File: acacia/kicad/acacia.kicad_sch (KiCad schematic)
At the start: 123 parts, among them J1 USB_C, SW1 A, SW10 C, SW11 R, SW12 F, SW13 V, SW14 T, SW15 G, SW16 Back, SW17 Gui, SW18 Ctl, SW19 Alt, SW2 Z, SW20 Sft, SW21 Fwd, SW22 AltGr, SW23 L1, SW24 L2, SW25 Ctl, SW26 U, SW27 J, SW28 M, SW29 H, SW3 Esc, SW30 N, SW31 I, SW32 K, SW33 Comm, SW34 O, SW35 L, SW36 Dot, SW37 QMK, SW38 P, SW39 Semi, SW4 B, SW40 Slsh, SW41 Y, SW42 Png, SW43 RESET, SW48 Q, SW49 RESET, SW5 W, SW6 S, SW7 X, SW8 E, SW9 D, U1 USBLC6-2SC6, U2 ATmega32U2-A, Y1 16MHz

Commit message: rearrange
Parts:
- removed FL1: CommonMode, symbol the_tree:Filter_EMI_CommonMode
- removed J1: USB_C, symbol Connector:USB_C_Receptacle_USB2.0
- removed SW37: QMK, symbol Switch:SW_Push_45deg
- added FL1: NCC0805F900KTRF, Inductor_SMD:L_CommonModeChoke_Coilcraft_0805USB, symbol mech-kbd:Filter_EMI_CommonMode
- added J1: USB4500-03-0-A, mech-kbd:USB4500030A, symbol mech-kbd:USB4500-03-0-A
- C1, C2, C3, C4, C5, C7, C8: footprint (none) -> Capacitor_SMD:C_0805_2012Metric_Pad1.18x1.45mm_HandSolder
- C6: footprint (none) -> Capacitor_SMD:C_1206_3216Metric_Pad1.33x1.80mm_HandSolder
- D1, D10, D11, D12, D13, D14, D15, D16, D17, D18, D19, D2, D20, D21, D22, D23, D24, D25, D26, D27, D28, D29, D3, D30, D31, D32, D33, D34, D35, D36, D37, D38, D39, D4, D40, D41, D48, D5, D6, D7, D8, D9: footprint (none) -> Diode_SMD:D_0805_2012Metric_Pad1.15x1.40mm_HandSolder
- F1: footprint (none) -> Resistor_SMD:R_1210_3225Metric_Pad1.30x2.65mm_HandSolder
- FB1, FB2, R1, R2, R3, R4, R5, R6, R7, R8: footprint (none) -> Resistor_SMD:R_0805_2012Metric_Pad1.20x1.40mm_HandSolder
- SW1, SW10, SW11, SW12, SW13, SW14, SW15, SW16, SW17, SW2, SW20, SW21, SW22, SW25, SW26, SW27, SW28, SW29, SW3, SW30, SW31, SW32, SW33, SW34, SW35, SW36, SW38, SW39, SW4, SW40, SW41, SW42, SW48, SW5, SW6, SW7, SW8, SW9: footprint (none) -> mech-kbd:MX-Hotswap-1U
- SW18, SW23, Y1: footprint (none) -> mech-kbd:MX-Hotswap-1.5U
- SW19, SW24: footprint (none) -> mech-kbd:MX-Hotswap-1.25U
- SW43: value RESET -> QMK; footprint (none) -> Button_Switch_SMD:SW_SPST_EVQQ2
- SW49: footprint (none) -> Button_Switch_SMD:SW_SPST_EVQQ2
- TP1, TP2: footprint (none) -> TestPoint:TestPoint_Pad_1.0x1.0mm
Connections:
- net D+: now also J1.A6 (DP1), J1.B6 (DP2)
- net D-: now also J1.A7 (DN1), J1.B7 (DN2)
- net DD+: now also FL1.4
- net DD-: now also FL1.1
- net GND: now also J1.A1 (GND_1), J1.A12 (GND_2)
- net GNDPWR: now also J1.MH1, J1.MH2, J1.MH3, J1.MH4
- net VBUS: now reaches FB2.1, U1.5 (VBUS)
- net VBUS: now also J1.A4 (VBUS_1), J1.A9 (VBUS_2)
- net at R8.1: now also J1.B5 (CC2)
- net at R7.1: now also J1.A5 (CC1)
- net at R3.1: now also FL1.2
- net at R2.1: now also FL1.3
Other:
- moved on the sheet: H1

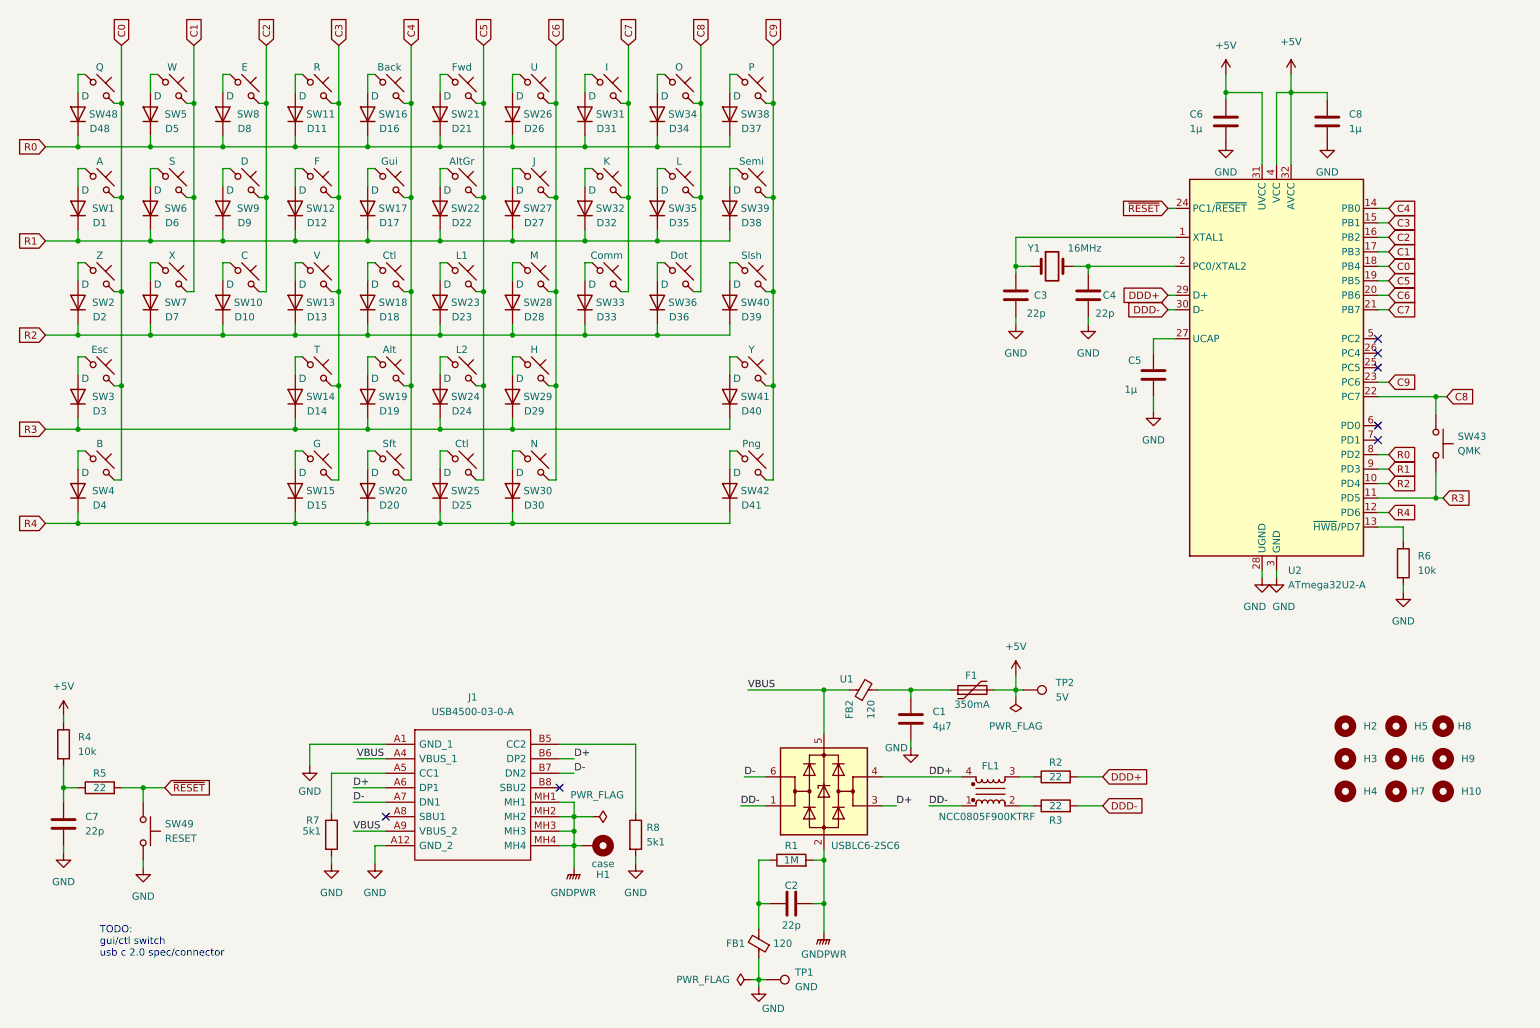
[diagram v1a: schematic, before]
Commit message: keys layed out
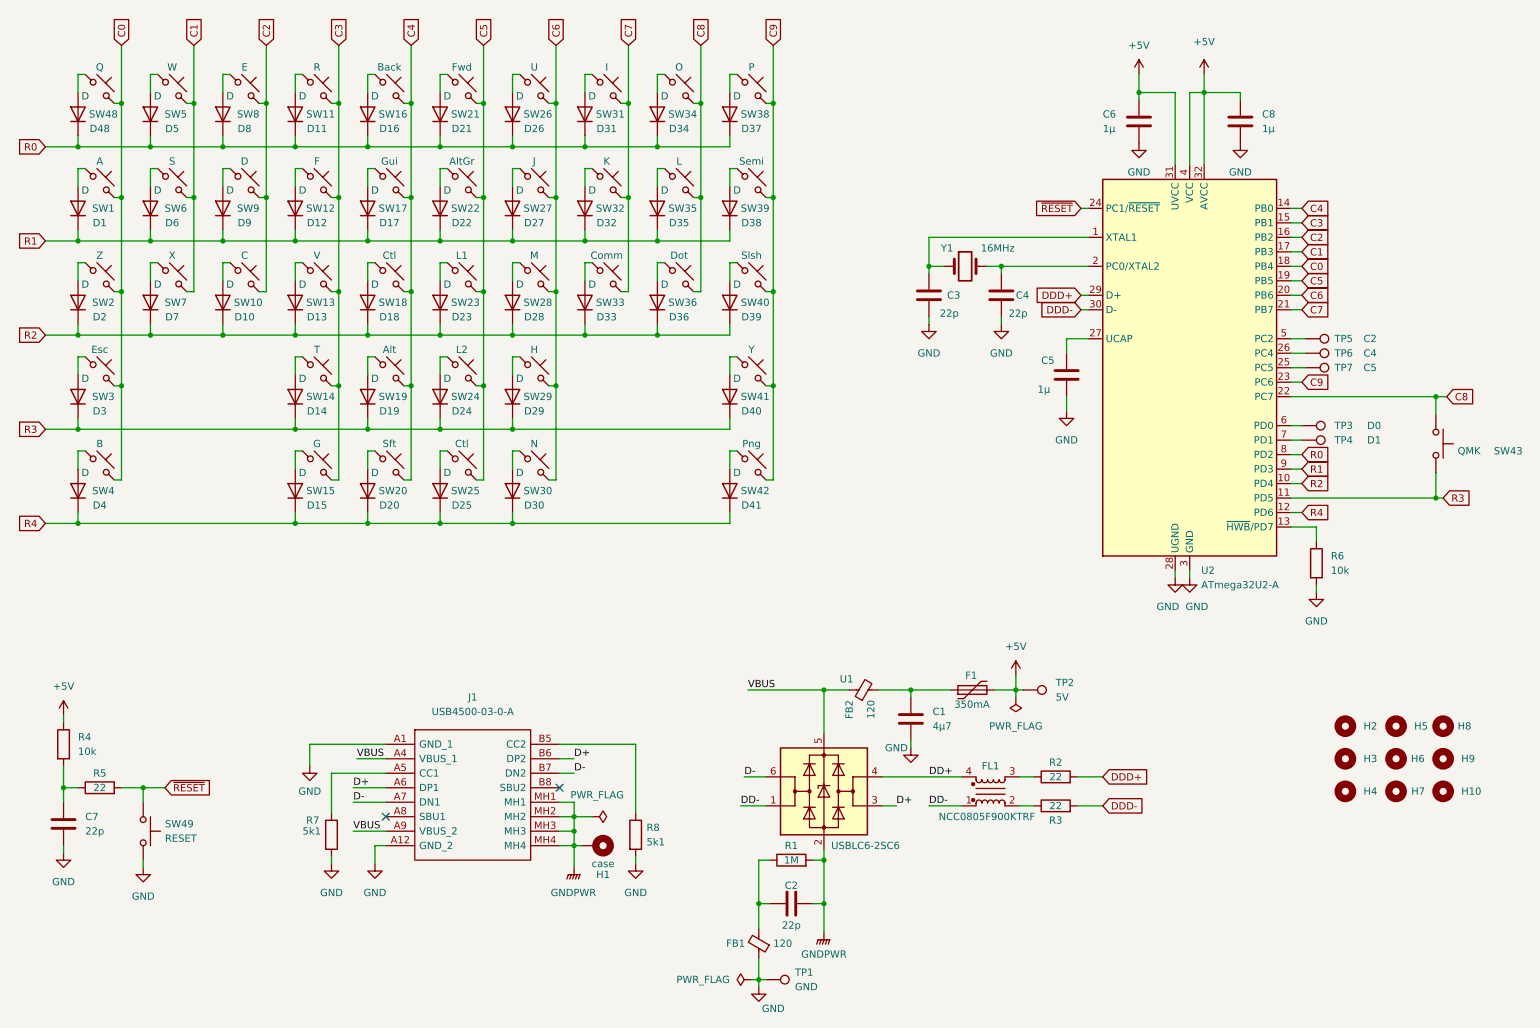
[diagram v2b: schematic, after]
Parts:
- added TP3: D0, TestPoint:TestPoint_Pad_1.0x1.0mm, symbol Connector:TestPoint
- added TP4: D1, TestPoint:TestPoint_Pad_1.0x1.0mm, symbol Connector:TestPoint
- added TP5: C2, TestPoint:TestPoint_Pad_1.0x1.0mm, symbol Connector:TestPoint
- added TP6: C4, TestPoint:TestPoint_Pad_1.0x1.0mm, symbol Connector:TestPoint
- added TP7: C5, TestPoint:TestPoint_Pad_1.0x1.0mm, symbol Connector:TestPoint
- Y1: footprint mech-kbd:MX-Hotswap-1.5U -> Crystal:Crystal_SMD_HC49-SD
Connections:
- net at U2.25 (PC5): now also TP7.1
- net at U2.26 (PC4): now also TP6.1
- net at U2.5 (PC2): now also TP5.1
- net at U2.6 (PD0): now also TP3.1
- net at U2.7 (PD1): now also TP4.1
- no-connect marks 7 -> 2
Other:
- note removed: "TODO: gui/ctl switch usb c 2.0 spec/connector"
- moved on the sheet: C3, C4, C5, C6, C8, R6, U2, Y1

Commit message: wip
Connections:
- net D-: now also U1.1 (I/O1); no longer U1.6 (I/O1)
- net DD+: now also FL1.3; no longer FL1.4
- net DD-: now also FL1.2, U1.6 (I/O1); no longer FL1.1, U1.1 (I/O1)
- net DDD+: now also R3.2; no longer R2.2
- net DDD-: now also R2.2; no longer R3.2
- net at R3.1: now also FL1.4; no longer FL1.2
- net at R2.1: now also FL1.1; no longer FL1.3
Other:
- moved on the sheet: FL1, R2, R3
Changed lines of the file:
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@@
     (stroke (width 0) (type default) (color 0 0 0 0))
   )
-  (wire (pts (xy 144.145 148.59) (xy 147.955 148.59))
+  (wire (pts (xy 142.875 148.59) (xy 147.955 148.59))
     (stroke (width 0) (type default) (color 0 0 0 0))
   )
@@
     (stroke (width 0) (type default) (color 0 0 0 0))
   )
-  (wire (pts (xy 143.51 153.67) (xy 147.955 153.67))
+  (wire (pts (xy 142.875 153.67) (xy 147.955 153.67))
     (stroke (width 0) (type default) (color 0 0 0 0))
   )
@@
     (stroke (width 0) (type default) (color 0 0 0 0))
   )
+  (wire (pts (xy 175.895 148.59) (xy 175.895 153.67))
+    (stroke (width 0) (type default) (color 0 0 0 0))
+  )
   (wire (pts (xy 27.305 104.14) (xy 65.405 104.14))
     (stroke (width 0) (type default) (color 0 0 0 0))
@@
     (stroke (width 0) (type default) (color 0 0 0 0))
   )
+  (wire (pts (xy 175.895 153.67) (xy 184.785 153.67))
+    (stroke (width 0) (type default) (color 0 0 0 0))
+  )
   (wire (pts (xy 147.955 30.48) (xy 149.225 30.48))
     (stroke (width 0) (type default) (color 0 0 0 0))
@@
     (stroke (width 0) (type default) (color 0 0 0 0))
   )
-  (wire (pts (xy 192.405 153.67) (xy 194.945 153.67))
+  (wire (pts (xy 194.945 153.67) (xy 197.485 153.67))
     (stroke (width 0) (type default) (color 0 0 0 0))
   )
@@
     (stroke (width 0) (type default) (color 0 0 0 0))
   )
-  (wire (pts (xy 202.565 153.67) (xy 207.01 153.67))
+  (wire (pts (xy 205.105 153.67) (xy 209.55 153.67))
     (stroke (width 0) (type default) (color 0 0 0 0))
   )
@@
     (stroke (width 0) (type default) (color 0 0 0 0))
   )
-  (wire (pts (xy 202.565 148.59) (xy 207.01 148.59))
+  (wire (pts (xy 205.105 148.59) (xy 209.55 148.59))
     (stroke (width 0) (type default) (color 0 0 0 0))
   )
@@
     (stroke (width 0) (type default) (color 0 0 0 0))
   )
-  (wire (pts (xy 192.405 148.59) (xy 194.945 148.59))
+  (wire (pts (xy 194.945 148.59) (xy 197.485 148.59))
     (stroke (width 0) (type default) (color 0 0 0 0))
   )
@@
     (stroke (width 0) (type default) (color 0 0 0 0))
   )
-  (wire (pts (xy 176.53 153.67) (xy 182.245 153.67))
+  (wire (pts (xy 179.705 148.59) (xy 184.785 148.59))
     (stroke (width 0) (type default) (color 0 0 0 0))
   )
@@
     (stroke (width 0) (type default) (color 0 0 0 0))
   )
-  (wire (pts (xy 168.275 148.59) (xy 182.245 148.59))
+  (wire (pts (xy 168.275 148.59) (xy 175.895 148.59))
     (stroke (width 0) (type default) (color 0 0 0 0))
   )
@@
     (stroke (width 0) (type default) (color 0 0 0 0))
   )
-  (label "DD+" (at 176.53 148.59 0)
+  (label "DD+" (at 171.45 148.59 0)
     (effects (font (size 1.27 1.27)) (justify left bottom))
   )
@@
     (effects (font (size 1.27 1.27)) (justify left bottom))
   )
-  (label "DD-" (at 143.51 153.67 0)
+  (label "DD-" (at 142.875 148.59 0)
     (effects (font (size 1.27 1.27)) (justify left bottom))
   )
@@
     (effects (font (size 1.27 1.27)) (justify left bottom))
   )
-  (label "D-" (at 144.145 148.59 0)
+  (label "D-" (at 142.875 153.67 0)
     (effects (font (size 1.27 1.27)) (justify left bottom))
   )
@@
     (effects (font (size 1.27 1.27)) (justify left bottom))
   )
-  (label "DD-" (at 176.53 153.67 0)
+  (label "DD-" (at 179.705 148.59 0)
     (effects (font (size 1.27 1.27)) (justify left bottom))
   )
@@
     )
   )
-  (global_label "DDD-" (shape input) (at 207.01 153.67 0) (fields_autoplaced)
+  (global_label "DDD-" (shape input) (at 209.55 148.59 0) (fields_autoplaced)
     (effects (font (size 1.27 1.27)) (justify left))
-    (property "Intersheet References" "${INTERSHEET_REFS}" (id 0) (at 214.8055 153.5906 0)
+    (property "Intersheet References" "${INTERSHEET_REFS}" (id 0) (at 217.3455 148.5106 0)
       (effects (font (size 1.27 1.27)) (justify left) hide)
     )
@@
     )
   )
-  (global_label "DDD+" (shape input) (at 207.01 148.59 0) (fields_autoplaced)
+  (global_label "DDD+" (shape input) (at 209.55 153.67 0) (fields_autoplaced)
     (effects (font (size 1.27 1.27)) (justify left))
-    (property "Intersheet References" "${INTERSHEET_REFS}" (id 0) (at 214.8055 148.5106 0)
+    (property "Intersheet References" "${INTERSHEET_REFS}" (id 0) (at 217.3455 153.5906 0)
       (effects (font (size 1.27 1.27)) (justify left) hide)
     )
@@
     (pin "2")
   )
-  (symbol (lib_id "mech-kbd:Filter_EMI_CommonMode") (at 187.325 151.13 0) (mirror x) (unit 1)
-    (in_bom yes) (on_board yes)
-    (property "Reference" "FL1" (id 0) (at 187.325 146.685 0))
-    (property "Value" "NCC0805F900KTRF" (id 1) (at 186.69 155.575 0))
-    (property "Footprint" "Inductor_SMD:L_CommonModeChoke_Coilcraft_0805USB" (id 2) (at 187.325 152.146 0)
-      (effects (font (size 1.27 1.27)) hide)
-    )
-    (property "Datasheet" "~" (id 3) (at 187.325 152.146 0)
+  (symbol (lib_id "mech-kbd:Filter_EMI_CommonMode") (at 189.865 151.13 0) (mirror y) (unit 1)
+    (in_bom yes) (on_board yes)
+    (property "Reference" "FL1" (id 0) (at 189.865 155.575 0))
+    (property "Value" "NCC0805F900KTRF" (id 1) (at 189.865 157.48 0))
+    (property "Footprint" "Inductor_SMD:L_CommonModeChoke_Coilcraft_0805USB" (id 2) (at 189.865 150.114 0)
+      (effects (font (size 1.27 1.27)) hide)
+    )
+    (property "Datasheet" "~" (id 3) (at 189.865 150.114 0)
       (effects (font (size 1.27 1.27)) hide)
     )
@@
     (pin "2")
   )
-  (symbol (lib_id "Device:R") (at 198.755 153.67 90) (unit 1)
-    (in_bom yes) (on_board yes)
-    (property "Reference" "R3" (id 0) (at 198.755 156.21 90))
-    (property "Value" "22" (id 1) (at 198.755 153.67 90))
-    (property "Footprint" "Resistor_SMD:R_0805_2012Metric_Pad1.20x1.40mm_HandSolder" (id 2) (at 198.755 155.448 90)
-      (effects (font (size 1.27 1.27)) hide)
-    )
-    (property "Datasheet" "~" (id 3) (at 198.755 153.67 0)
+  (symbol (lib_id "Device:R") (at 201.295 153.67 90) (unit 1)
+    (in_bom yes) (on_board yes)
+    (property "Reference" "R3" (id 0) (at 201.295 156.21 90))
+    (property "Value" "22" (id 1) (at 201.295 153.67 90))
+    (property "Footprint" "Resistor_SMD:R_0805_2012Metric_Pad1.20x1.40mm_HandSolder" (id 2) (at 201.295 155.448 90)
+      (effects (font (size 1.27 1.27)) hide)
+    )
+    (property "Datasheet" "~" (id 3) (at 201.295 153.67 0)
       (effects (font (size 1.27 1.27)) hide)
     )
@@
     (pin "2")
   )
-  (symbol (lib_id "Device:R") (at 198.755 148.59 90) (unit 1)
-    (in_bom yes) (on_board yes)
-    (property "Reference" "R2" (id 0) (at 198.755 146.05 90))
-    (property "Value" "22" (id 1) (at 198.755 148.59 90))
-    (property "Footprint" "Resistor_SMD:R_0805_2012Metric_Pad1.20x1.40mm_HandSolder" (id 2) (at 198.755 150.368 90)
-      (effects (font (size 1.27 1.27)) hide)
-    )
-    (property "Datasheet" "~" (id 3) (at 198.755 148.59 0)
-      (effects (font (size 1.27 1.27)) hide)
-    )
+  (symbol (lib_id "Device:R") (at 201.295 148.59 90) (unit 1)
+    (in_bom yes) (on_board yes)
+    (property "Reference" "R2" (id 0) (at 201.295 146.05 90))
+    (property "Value" "22" (id 1) (at 201.295 148.59 90))
+    (property "Footprint" "Resistor_SMD:R_0805_2012Metric_Pad1.20x1.40mm_HandSolder" (id 2) (at 201.295 150.368 90)
+      (effects (font (size 1.27 1.27)) hide)
+    )
+    (property "Datasheet" "~" (id 3) (at 201.295 148.59 0)
+      (effects (font (size 1.27 1.27)) hide)
+    )
